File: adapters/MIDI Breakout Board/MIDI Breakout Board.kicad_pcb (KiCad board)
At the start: 2 copper layers, 41.4 x 47.3 mm, 14 parts, among them J1 MIDI, J2 MIDI OUT, J3 MIDI IN, M1 Mounting_Pin, M2 Mounting_Pin, U1 6N138, U3 74LS00

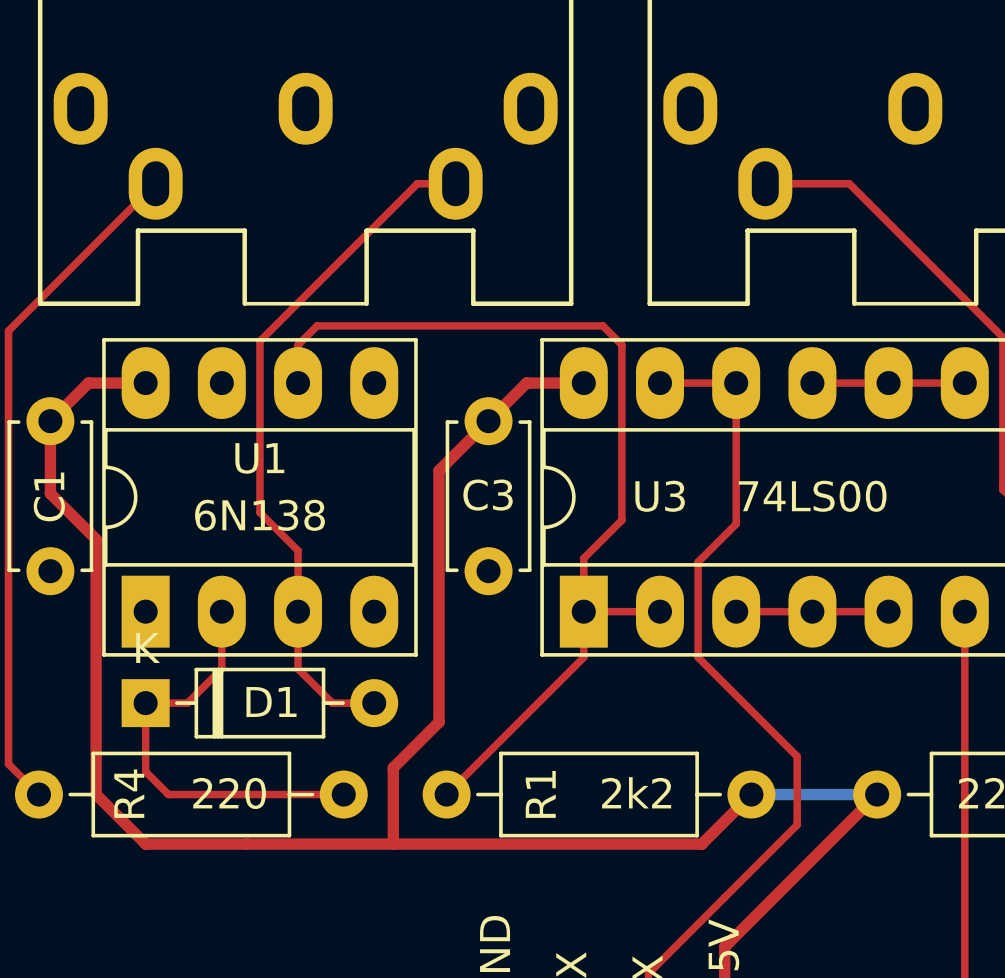
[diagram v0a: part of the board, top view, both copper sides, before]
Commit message: Add pulldown to breakout board
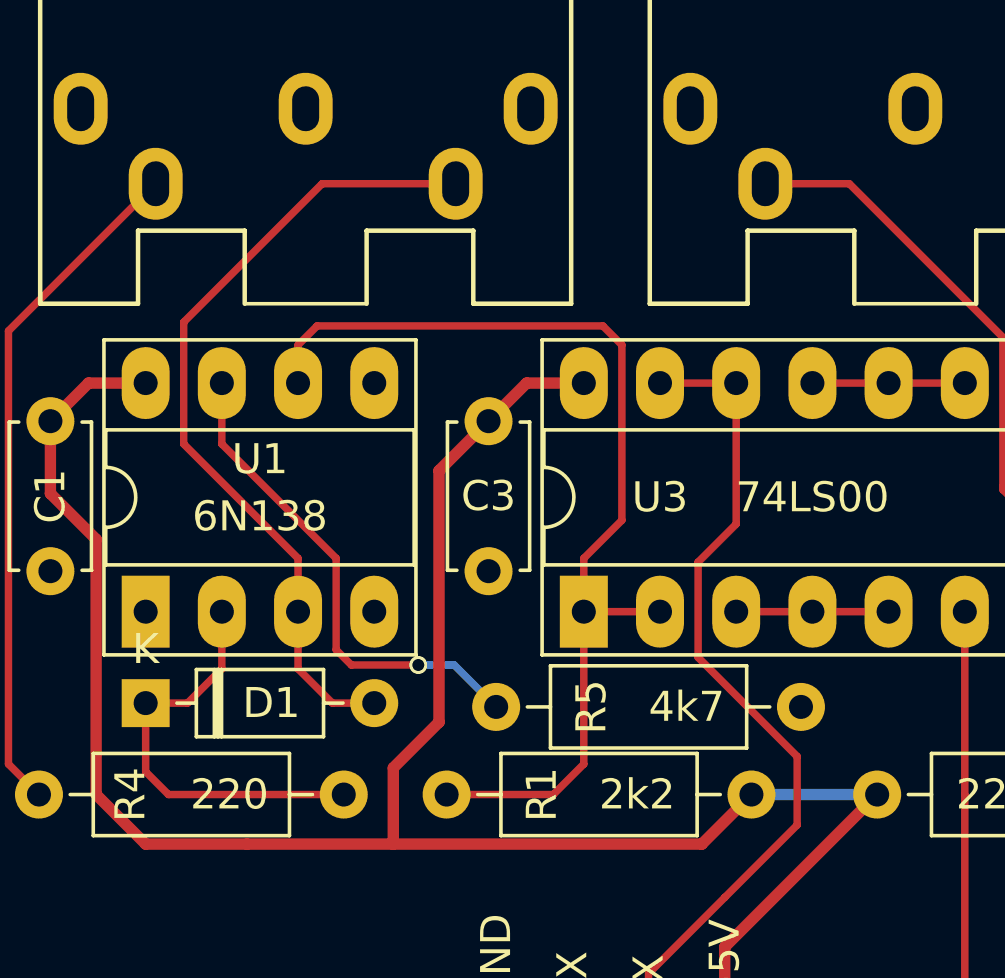
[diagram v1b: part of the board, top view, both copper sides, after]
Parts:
- added R5: 4k7, Resistor_THT:R_Axial_DIN0207_L6.3mm_D2.5mm_P10.16mm_Horizontal, F.Cu at (124.5, 99.7)
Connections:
- U1 pad 7: (no net) -> Net-(R5-Pad2)
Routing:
- net Net-(R5-Pad2): track 0.00 -> 16.6 mm, vias 0 -> 1
- net Net-(D1-Pad2): track 23.2 -> 27.1 mm
- net Net-(R1-Pad2): track 32.5 -> 34.6 mm
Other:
- board text added: "BulkyMIDI-32 MIDI Breakout (rev. B) github.com/tebl"
- board text removed: "BulkyMIDI-32 MIDI Breakout (rev. A) github.com/tebl"
